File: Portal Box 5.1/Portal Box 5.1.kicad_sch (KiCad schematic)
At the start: 80 parts, among them J1 609-87520-0010ALFCT-ND, J2 2073-USB4105-GF-ACT-ND, J3 A 14-LC-TT, J4 732-6001-1-ND, J5 RFID-RC522, J6 Conn_01x04, K1 PR28-5V-360-1A-E, K2 DIP05-2A72-21L, Q1 NTR5103NT1G, Q2 NTR5103NT1G, SW1 141-TL3336AF160QCT-ND, SW2 SW_DPST, U1 497-5026-1-ND, U2 497-5026-1-ND, U3 448-TLE4971A050T5UE0001XUMA1C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, U4 AP7363-33D-13, U5 ESP32-S3-DEVKITC-1-N8R8-OFFIC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

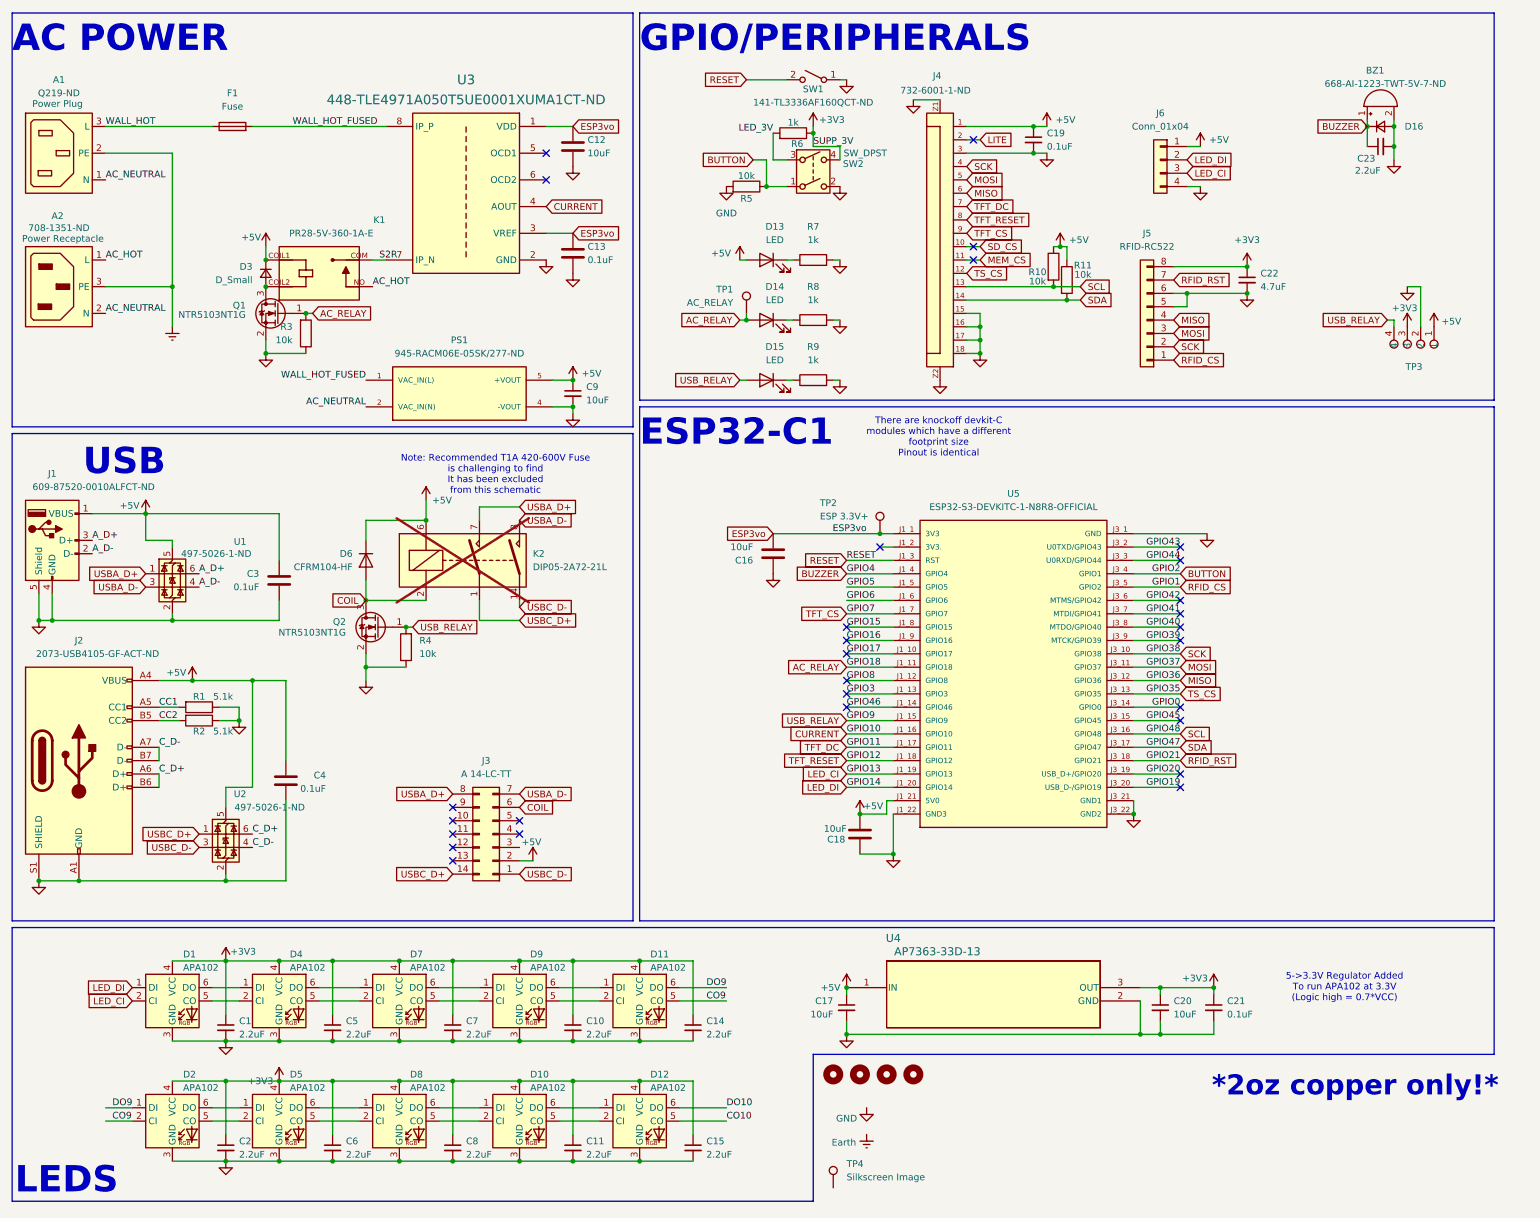
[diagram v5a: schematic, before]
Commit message: schematic updates, added ground jumper
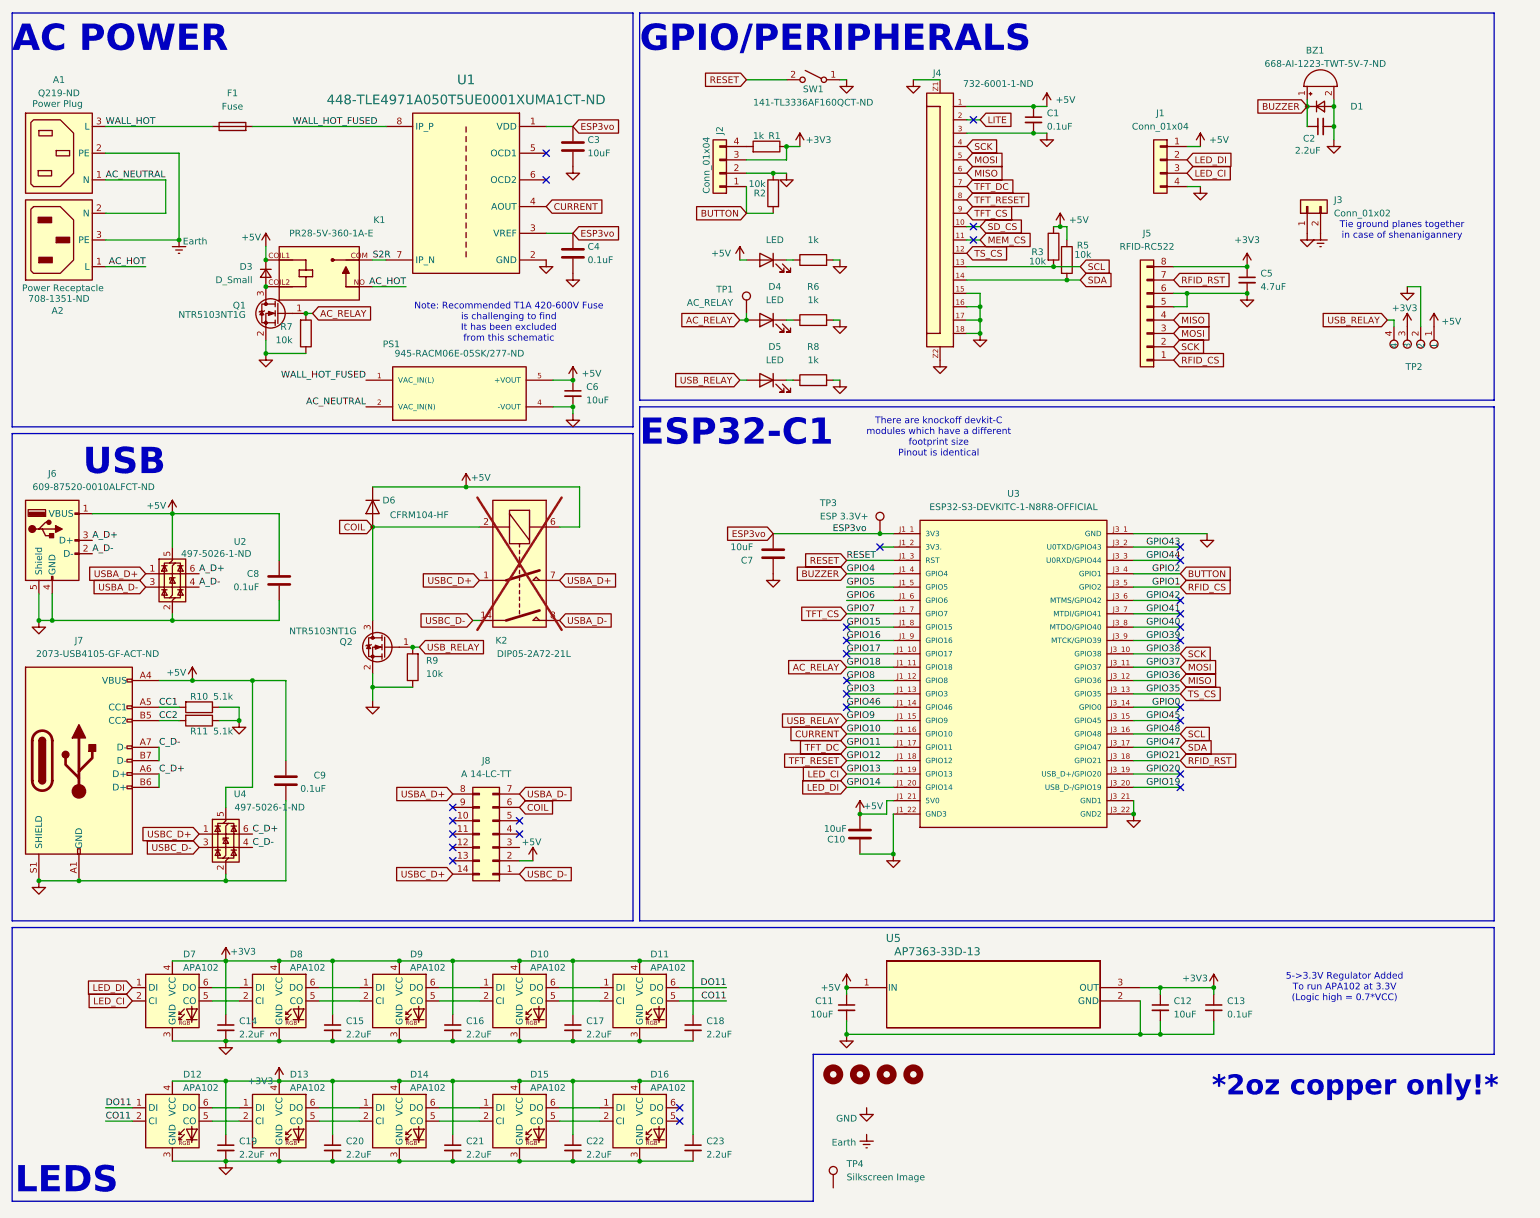
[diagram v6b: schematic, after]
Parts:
- removed R5: 10k, Resistor_SMD:R_0805_2012Metric, symbol Device:R
- removed R6: 1k, Resistor_SMD:R_0805_2012Metric, symbol Device:R
- removed SW2: SW_DPST, Connector_PinHeader_2.54mm:PinHeader_1x04_P2.54mm_Vertical, symbol Switch:SW_DPST
- added J2: Conn_01x04, Connector_PinHeader_2.54mm:PinHeader_1x04_P2.54mm_Vertical, symbol Connector_Generic:Conn_01x04
- added J3: Conn_01x02, Connector_PinHeader_2.54mm:PinHeader_1x02_P2.54mm_Vertical, symbol Connector_Generic:Conn_01x02
- added R1: 1k, Resistor_SMD:R_0805_2012Metric, symbol Device:R
- added R2: 10k, Resistor_SMD:R_0805_2012Metric, symbol Device:R
- renumbered C19 to C1, C18 to C10, C17 to C11, C20 to C12, C21 to C13, C1 to C14, C5 to C15, C7 to C16, C10 to C17, C14 to C18, C2 to C19, C23 to C2, C6 to C20, C8 to C21, C11 to C22, C15 to C23, C12 to C3, C13 to C4, C22 to C5, C9 to C6, C16 to C7, C3 to C8, C4 to C9, D16 to D1, D9 to D10, D2 to D12, D5 to D13, D8 to D14, D10 to D15, D12 to D16, D13 to D2, D14 to D4, D15 to D5, D1 to D7, D4 to D8, D7 to D9, J6 to J1, J1 to J6, J2 to J7, J3 to J8, R1 to R10, R2 to R11, R10 to R3, R7 to R4, R11 to R5, R8 to R6, R3 to R7, R9 to R8, R4 to R9, TP3 to TP2, TP2 to TP3, U3 to U1, U1 to U2, U5 to U3, U2 to U4, U4 to U5
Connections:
- net +3V3: now also J2.3 (Pin_3), R1.1
- net BUTTON: now also J2.1 (Pin_1), R2.2
- net Earth: now also J3.2 (Pin_2)
- net GND: now also J2.2 (Pin_2), J3.1 (Pin_1), R2.1
- net CO10: no longer names the net of D16.5 (CO)
- net CO9 renamed CO11
- net DO10: no longer names the net of D16.6 (DO)
- net DO9 renamed DO11
- new net: J2.4 (Pin_4), R1.2
- no-connect marks 29 -> 31
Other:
- note added: "Tie ground planes together in case of shenanigannery"
- moved on the sheet: A2, BZ1, C1, C2, D1, D6, J4, K2, Q2, R3, R5, R9

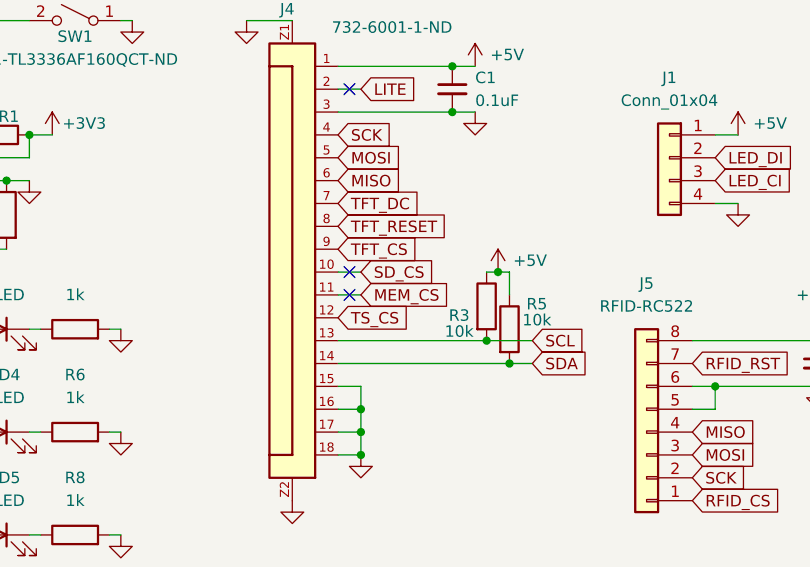
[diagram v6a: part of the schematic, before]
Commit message: update component labels
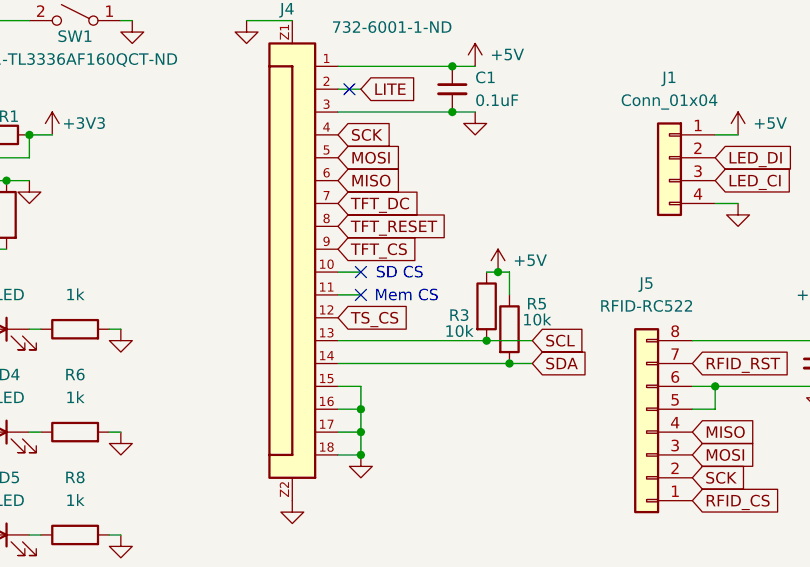
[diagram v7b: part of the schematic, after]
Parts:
- A1: Label (none) -> WALL IN
- A2: Label (none) -> WALL OUT
- BZ1: Label (none) -> BUZZER
- D2: Label (none) -> PWR
- D4: Label (none) -> AC RELAY
- D5: Label (none) -> USB
- F1: Label (none) -> FUSE
- J1: Label (none) -> LED
- J2: Label (none) -> BUTTON
- J4: Label (none) -> RIBBON CABLE
- J5: Label (none) -> RFID
- J6: Label (none) -> USB-A
- J7: Label (none) -> USB-C
- J8: Label (none) -> USB RELAY
- K1: Label (none) -> PWR RELAY
- PS1: Label (none) -> AC/DC
- SW1: Label (none) -> RST
- TP3: Label (none) -> ESP 3v3
- U1: Label (none) -> CURRENT MEAS
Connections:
- net MEM_CS: no longer names the net of J4.11
- net SD_CS: no longer names the net of J4.10
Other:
- note added: "Mem CS"
- note added: "SD CS"
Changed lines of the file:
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@@
 		)
 	)
+	(text "Mem CS"
+		(exclude_from_sim no)
+		(at 203.2 59.944 0)
+		(effects
+			(font
+				(size 1.27 1.27)
+			)
+		)
+	)
 	(text "5->3.3V Regulator Added\nTo run APA102 at 3.3V\n(Logic high = 0.7*VCC)"
 		(exclude_from_sim no)
@@
 		)
 	)
+	(text "SD CS"
+		(exclude_from_sim no)
+		(at 202.438 57.404 0)
+		(effects
+			(font
+				(size 1.27 1.27)
+			)
+		)
+	)
 	(text "GPIO/PERIPHERALS"
 		(exclude_from_sim no)
@@
 	)
 	(no_connect
-		(at 196.85 59.69)
+		(at 198.12 59.69)
 	)
 	(no_connect
@@
 	)
 	(no_connect
-		(at 196.85 57.15)
+		(at 198.12 57.15)
 	)
 	(no_connect
@@
 		)
 	)
-	(global_label "MEM_CS"
-		(shape input)
-		(at 198.12 59.69 0)
-		(fields_autoplaced yes)
-		(effects
-			(font
-				(size 1.27 1.27)
-			)
-			(justify left)
-		)
-		(property "Intersheetrefs" "${INTERSHEET_REFS}"
-			(at 208.6041 59.69 0)
-			(effects
-				(font
-					(size 1.27 1.27)
-				)
-				(justify left)
-				(hide yes)
-			)
-		)
-	)
 	(global_label "USBC_D+"
 		(shape input)
@@
 		)
 	)
-	(global_label "SD_CS"
-		(shape input)
-		(at 198.12 57.15 0)
-		(fields_autoplaced yes)
-		(effects
-			(font
-				(size 1.27 1.27)
-			)
-			(justify left)
-		)
-		(property "Intersheetrefs" "${INTERSHEET_REFS}"
-			(at 207.0318 57.15 0)
-			(effects
-				(font
-					(size 1.27 1.27)
-				)
-				(justify left)
-				(hide yes)
-			)
-		)
-	)
 	(global_label "ESP3vo"
 		(shape input)
@@
 			)
 		)
+		(property "Label" "WALL OUT"
+			(at 22.86 59.69 0)
+			(effects
+				(font
+					(size 1.27 1.27)
+				)
+				(hide yes)
+			)
+		)
 		(pin "3"
 		)
@@
 			)
 		)
+		(property "Label" "AC RELAY"
+			(at 157.48 74.93 0)
+			(effects
+				(font
+					(size 1.27 1.27)
+				)
+				(hide yes)
+			)
+		)
 		(pin "2"
 		)
@@
 			)
 		)
+		(property "Label" "LED"
+			(at 232.41 44.45 0)
+			(effects
+				(font
+					(size 1.27 1.27)
+				)
+				(hide yes)
+			)
+		)
 		(pin "4"
 		)
@@
 			)
 		)
+		(property "Label" "RST"
+			(at 166.37 29.21 0)
+			(effects
+				(font
+					(size 1.27 1.27)
+				)
+				(hide yes)
+			)
+		)
 		(pin "1"
 		)
@@
 			)
 		)
+		(property "Label" "USB"
+			(at 157.48 86.36 0)
+			(effects
+				(font
+					(size 1.27 1.27)
+				)
+				(hide yes)
+			)
+		)
 		(pin "2"
 		)
@@
 			)
 		)
+		(property "Label" "USB-C"
+			(at 26.67 158.75 0)
+			(effects
+				(font
+					(size 1.27 1.27)
+				)
+				(hide yes)
+			)
+		)
 		(pin "B7"
 		)
@@
 			)
 		)
+		(property "Label" "RFID"
+			(at 229.87 74.93 0)
+			(effects
+				(font
+					(size 1.27 1.27)
+				)
+				(hide yes)
+			)
+		)
 		(pin "2"
 		)
@@
 			)
 		)
+		(property "Label" "BUTTON"
+			(at 148.59 46.99 90)
+			(effects
+				(font
+					(size 1.27 1.27)
+				)
+				(hide yes)
+			)
+		)
 		(pin "4"
 		)
@@
 			)
 		)
+		(property "Label" "FUSE"
+			(at 55.88 38.1 90)
+			(effects
+				(font
+					(size 1.27 1.27)
+				)
+				(hide yes)
+			)
+		)
 		(pin "1"
 		)
@@
 			)
 		)
+		(property "Label" "WALL IN"
+			(at 22.86 43.18 0)
+			(effects
+				(font
+					(size 1.27 1.27)
+				)
+				(hide yes)
+			)
+		)
 		(pin "2"
 		)
@@
 			)
 		)
+		(property "Label" "CURRENT MEAS"
+			(at 90.17 35.56 0)
+			(effects
+				(font
+					(size 1.27 1.27)
+				)
+				(hide yes)
+			)
+		)
 		(pin "3"
 		)
@@
 			)
 		)
+		(property "Label" "AC/DC"
+			(at 99.06 88.9 0)
+			(effects
+				(font
+					(size 1.27 1.27)
+				)
+				(hide yes)
+			)
+		)
 		(pin "2"
 		)
@@
 			)
 		)
+		(property "Label" "RIBBON CABLE"
+			(at 190.5 54.61 90)
+			(effects
+				(font
+					(size 1.27 1.27)
+				)
+				(hide yes)
+			)
+		)
 		(pin "18"
 		)
@@
 			)
 		)
+		(property "Label" "ESP 3v3"
+			(at 179.07 115.57 0)
+			(effects
+				(font
+					(size 1.27 1.27)
+				)
+				(hide yes)
+			)
+		)
 		(pin "1"
 		)
@@
 			)
 		)
+		(property "Label" "BUZZER"
+			(at 262.89 30.48 90)
+			(effects
+				(font
+					(size 1.27 1.27)
+				)
+				(hide yes)
+			)
+		)
 		(pin "2"
 		)
@@
 			)
 		)
+		(property "Label" "PWR RELAY"
+			(at 72.39 66.04 0)
+			(effects
+				(font
+					(size 1.27 1.27)
+				)
+				(hide yes)
+			)
+		)
 		(pin "COIL2"
 		)
@@
 			)
 		)
+		(property "Label" "PWR"
+			(at 157.48 63.5 0)
+			(effects
+				(font
+					(size 1.27 1.27)
+				)
+				(hide yes)
+			)
+		)
 		(pin "2"
 		)
@@
 			)
 		)
+		(property "Label" "USB-A"
+			(at 21.59 116.84 0)
+			(effects
+				(font
+					(size 1.27 1.27)
+				)
+				(hide yes)
+			)
+		)
 		(pin "5"
 		)
@@
 			(at 105.41 172.72 0)
 			(effects
+				(font
+					(size 1.27 1.27)
+				)
+				(hide yes)
+			)
+		)
+		(property "Label" "USB RELAY"
+			(at 105.41 172.72 0)
+			(effects

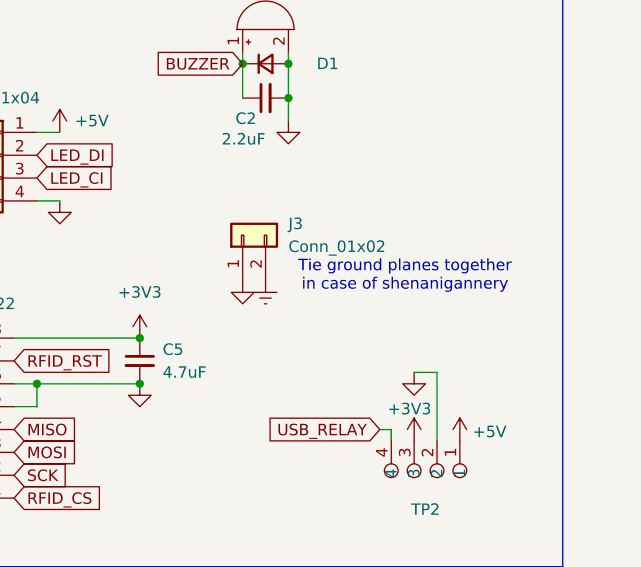
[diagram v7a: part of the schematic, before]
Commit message: chore: fix labels, solid pad connections, and version no.
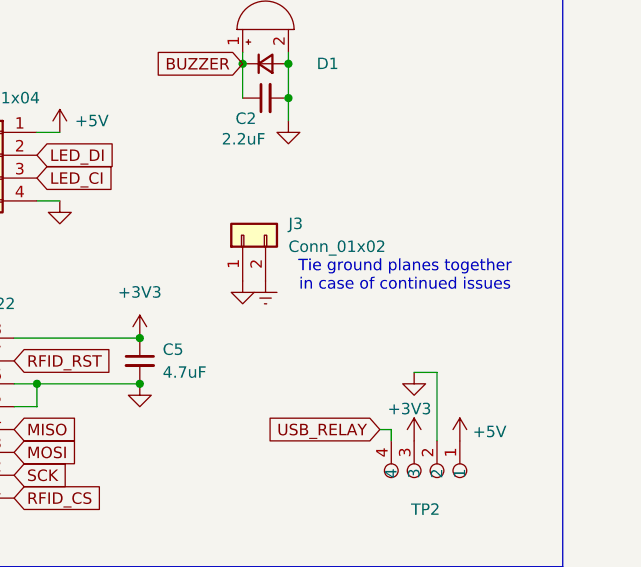
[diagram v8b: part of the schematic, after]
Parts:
- J3: Label (none) -> JMP; Label2 (none) -> GND
- J4: Label RIBBON CABLE -> RIBBON; Label2 (none) -> CABLE
- J8: Label USB RELAY -> USB; Label2 (none) -> RELAY
- K1: Label PWR RELAY -> PWR; Label2 (none) -> RELAY
- U1: Label CURRENT MEAS -> CURRENT; Label2 (none) -> MEAS
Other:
- note added: "Tie ground planes together in case of continued issues"
- note removed: "Tie ground planes together in case of shenanigannery"
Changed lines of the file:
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@@
 		(title "PortalBox Project")
 		(date "2025-10-25")
-		(rev "V5.1.1")
+		(rev "V5.1.2")
 		(company "Bucknell University | Electrical and Computer Engineering ")
 		(comment 1 "Aiden Cherniske & Elisha Foster")
@@
 		)
 	)
-	(text "Tie ground planes together\nin case of shenanigannery"
+	(text "Tie ground planes together\nin case of continued issues"
 		(exclude_from_sim no)
 		(at 278.384 57.912 0)
@@
 			)
 		)
-		(property "Label" "CURRENT MEAS"
+		(property "Label" "CURRENT"
+			(at 90.17 35.56 0)
+			(effects
+				(font
+					(size 1.27 1.27)
+				)
+				(hide yes)
+			)
+		)
+		(property "Label2" "MEAS"
 			(at 90.17 35.56 0)
 			(effects
@@
 			)
 		)
-		(property "Label" "RIBBON CABLE"
+		(property "Label" "RIBBON"
+			(at 190.5 54.61 90)
+			(effects
+				(font
+					(size 1.27 1.27)
+				)
+				(hide yes)
+			)
+		)
+		(property "Label2" "CABLE"
 			(at 190.5 54.61 90)
 			(effects
@@
 			)
 		)
+		(property "Label" "JMP"
+			(at 260.35 53.34 90)
+			(effects
+				(font
+					(size 1.27 1.27)
+				)
+				(hide yes)
+			)
+		)
+		(property "Label2" "GND"
+			(at 260.35 53.34 90)
+			(effects
+				(font
+					(size 1.27 1.27)
+				)
+				(hide yes)
+			)
+		)
 		(pin "2"
 		)
@@
 			)
 		)
-		(property "Label" "PWR RELAY"
+		(property "Label" "PWR"
+			(at 72.39 66.04 0)
+			(effects
+				(font
+					(size 1.27 1.27)
+				)
+				(hide yes)
+			)
+		)
+		(property "Label2" "RELAY"
 			(at 72.39 66.04 0)
 			(effects
@@
 			)
 		)
-		(property "Label" "USB RELAY"
+		(property "Label" "USB"
+			(at 105.41 172.72 0)
+			(effects
+				(font
+					(size 1.27 1.27)
+				)
+				(hide yes)
+			)
+		)
+		(property "Label2" "RELAY"
 			(at 105.41 172.72 0)
 			(effects
